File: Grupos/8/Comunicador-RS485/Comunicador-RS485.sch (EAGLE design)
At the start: 14 parts, among them P1 10k, T1 SN65HVD3082EDR

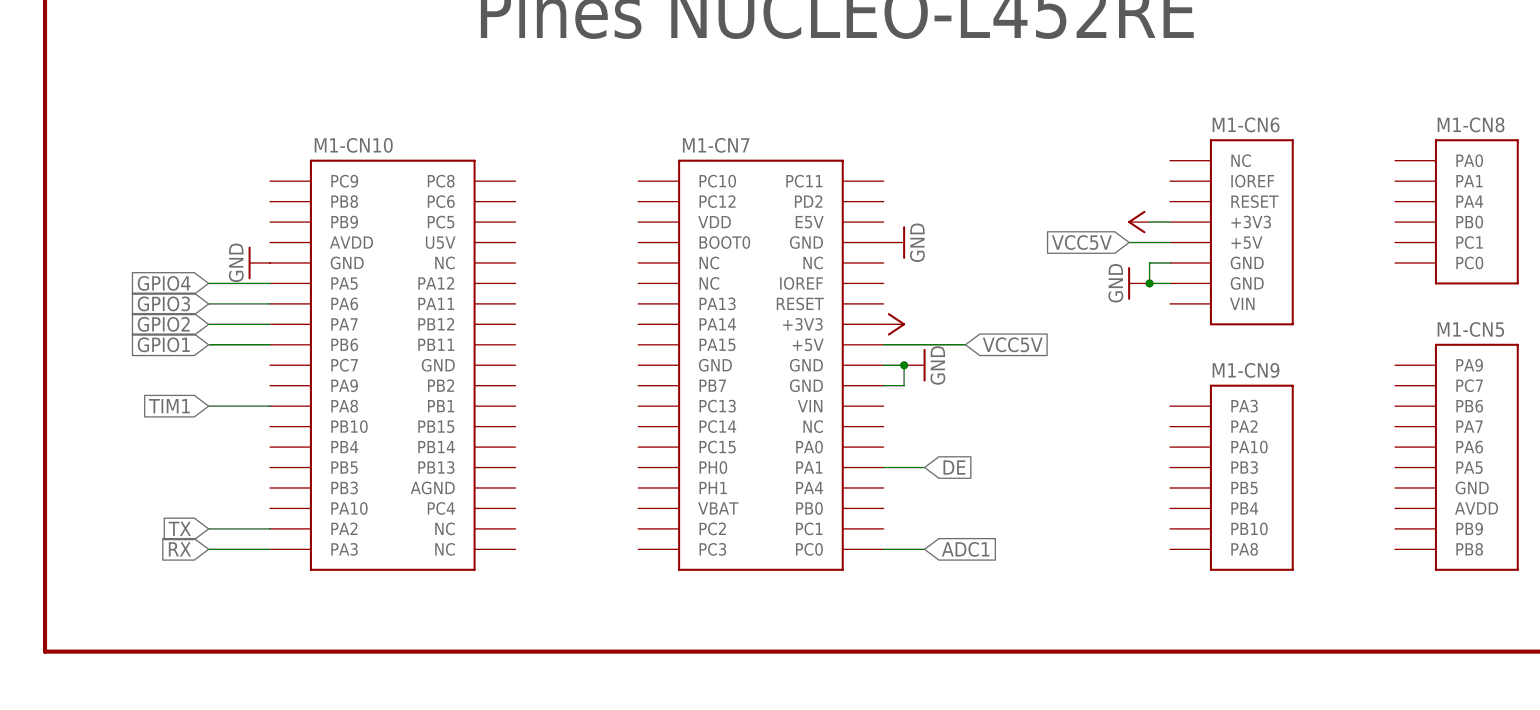
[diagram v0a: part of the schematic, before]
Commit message: Se mueve el RS485 a UART4
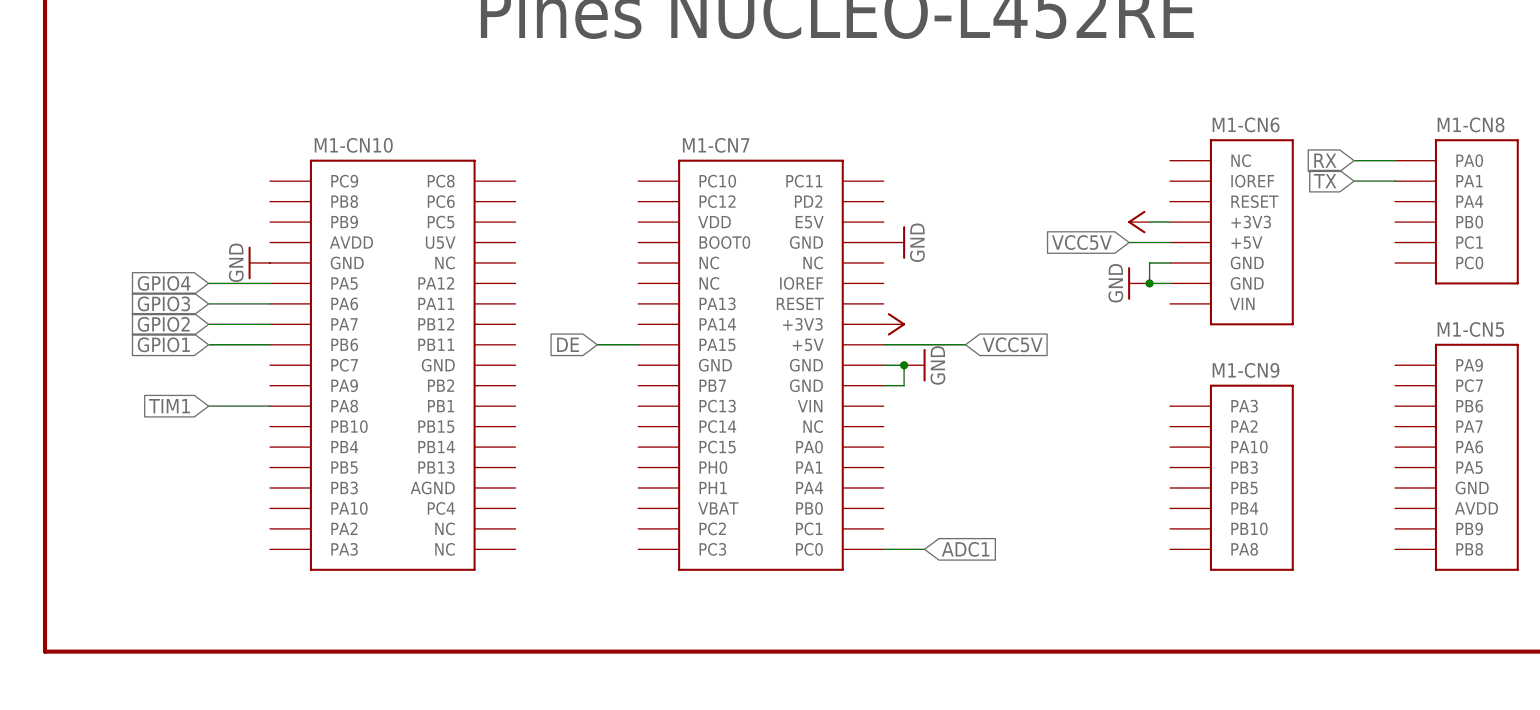
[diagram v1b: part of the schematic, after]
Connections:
- net DE: now also M1-CN7.PA15; no longer M1-CN7.PA1
- net RX: now also M1-CN8.PA0; no longer M1-CN10.PA3
- net TX: now also M1-CN8.PA1; no longer M1-CN10.PA2
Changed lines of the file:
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@@
 <drawing>
 <settings>
-<setting alwaysvectorfont="no"/>
+<setting alwaysvectorfont="yes"/>
 <setting verticaltext="up"/>
 </settings>
@@
 <net name="TX" class="0">
 <segment>
-<pinref part="M1" gate="-CN10" pin="PA2"/>
-<wire x1="45.72" y1="30.48" x2="38.1" y2="30.48" width="0.1524" layer="91"/>
-<label x="38.1" y="30.48" size="1.778" layer="95" rot="R180" xref="yes"/>
-</segment>
-<segment>
 <pinref part="T1" gate="BUFF" pin="D"/>
 <wire x1="-121.92" y1="-45.72" x2="-149.86" y2="-45.72" width="0.1524" layer="91"/>
 <label x="-149.86" y="-45.72" size="1.778" layer="95" rot="R180" xref="yes"/>
 </segment>
+<segment>
+<pinref part="M1" gate="-CN8" pin="PA1"/>
+<wire x1="180.34" y1="73.66" x2="185.42" y2="73.66" width="0.1524" layer="91"/>
+<label x="180.34" y="73.66" size="1.778" layer="95" rot="R180" xref="yes"/>
+</segment>
 </net>
 <net name="RX" class="0">
-<segment>
-<pinref part="M1" gate="-CN10" pin="PA3"/>
-<wire x1="45.72" y1="27.94" x2="38.1" y2="27.94" width="0.1524" layer="91"/>
-<label x="38.1" y="27.94" size="1.778" layer="95" rot="R180" xref="yes"/>
-</segment>
 <segment>
 <pinref part="R4" gate="G$1" pin="1"/>
@@
 <junction x="-137.16" y="-20.32"/>
 <label x="-149.86" y="-20.32" size="1.778" layer="95" rot="R180" xref="yes"/>
+</segment>
+<segment>
+<pinref part="M1" gate="-CN8" pin="PA0"/>
+<wire x1="185.42" y1="76.2" x2="180.34" y2="76.2" width="0.1524" layer="91"/>
+<label x="180.34" y="76.2" size="1.778" layer="95" rot="R180" xref="yes"/>
 </segment>
 </net>
@@
 </net>
 <net name="DE" class="0">
-<segment>
-<pinref part="M1" gate="-CN7" pin="PA1"/>
-<wire x1="127" y1="38.1" x2="121.92" y2="38.1" width="0.1524" layer="91"/>
-<label x="127" y="38.1" size="1.778" layer="95" xref="yes"/>
-</segment>
 <segment>
 <pinref part="T1" gate="BUFF" pin="RE"/>
@@
 <label x="-127" y="-53.34" size="1.778" layer="95" rot="R270" xref="yes"/>
 </segment>
-</net>
+<segment>
+<pinref part="M1" gate="-CN7" pin="PA15"/>
+<wire x1="91.44" y1="53.34" x2="86.36" y2="53.34" width="0.1524" layer="91"/>
+<label x="86.36" y="53.34" size="1.778" layer="95" rot="R180" xref="yes"/>
+</segment>
+</net>
